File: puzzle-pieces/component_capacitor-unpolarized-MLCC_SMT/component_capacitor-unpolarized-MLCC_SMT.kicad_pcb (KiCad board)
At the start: 2 copper layers, 40 x 40 mm, 34 parts, among them J1 Conn_01x02_Pin, J2 Conn_01x02_Pin

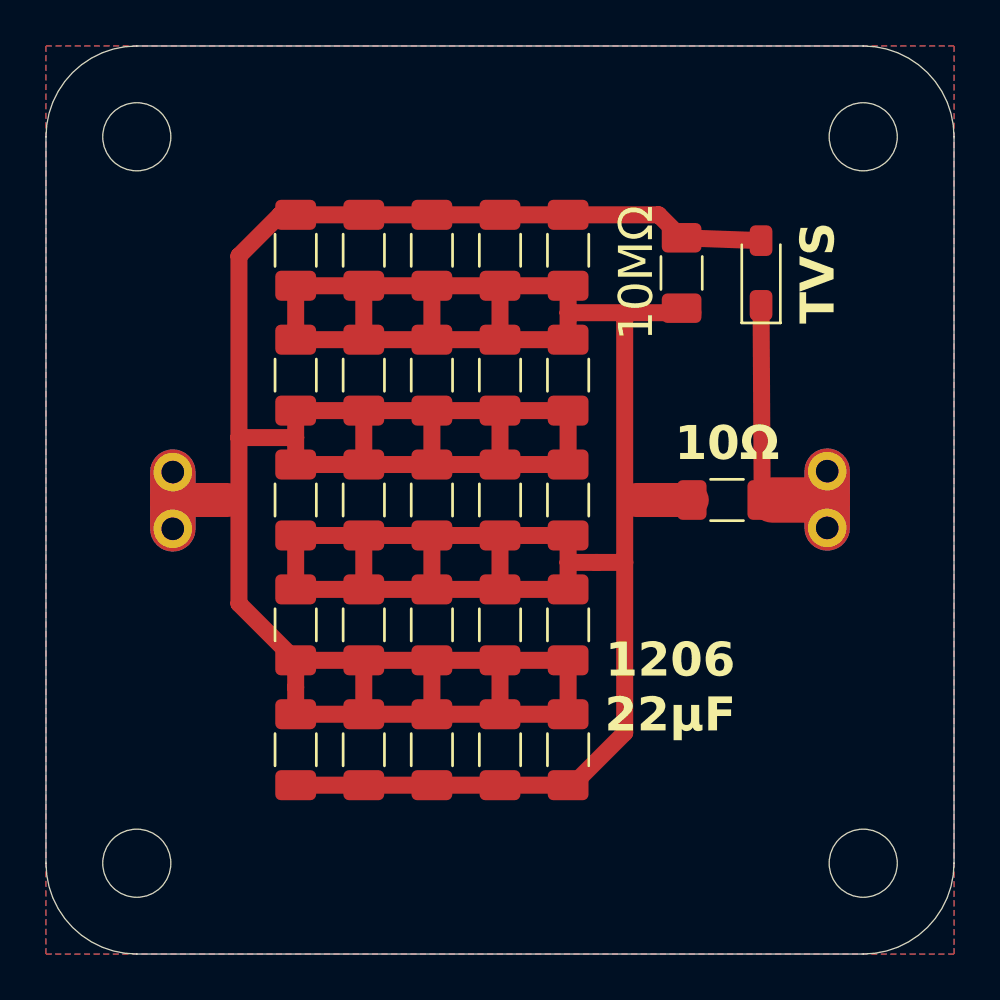
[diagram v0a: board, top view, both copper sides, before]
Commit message: Update unpolarized MLCC SMT components and kicad-viewer configuration
- Updated bottom and top PNG images for the unpolarized MLCC SMT component.
- Updated the ZIP file for the unpolarized MLCC SMT production assets.
- Modified kicad-viewer.json to include "fp_text" and "fp_values" layers in the rendering configuration.
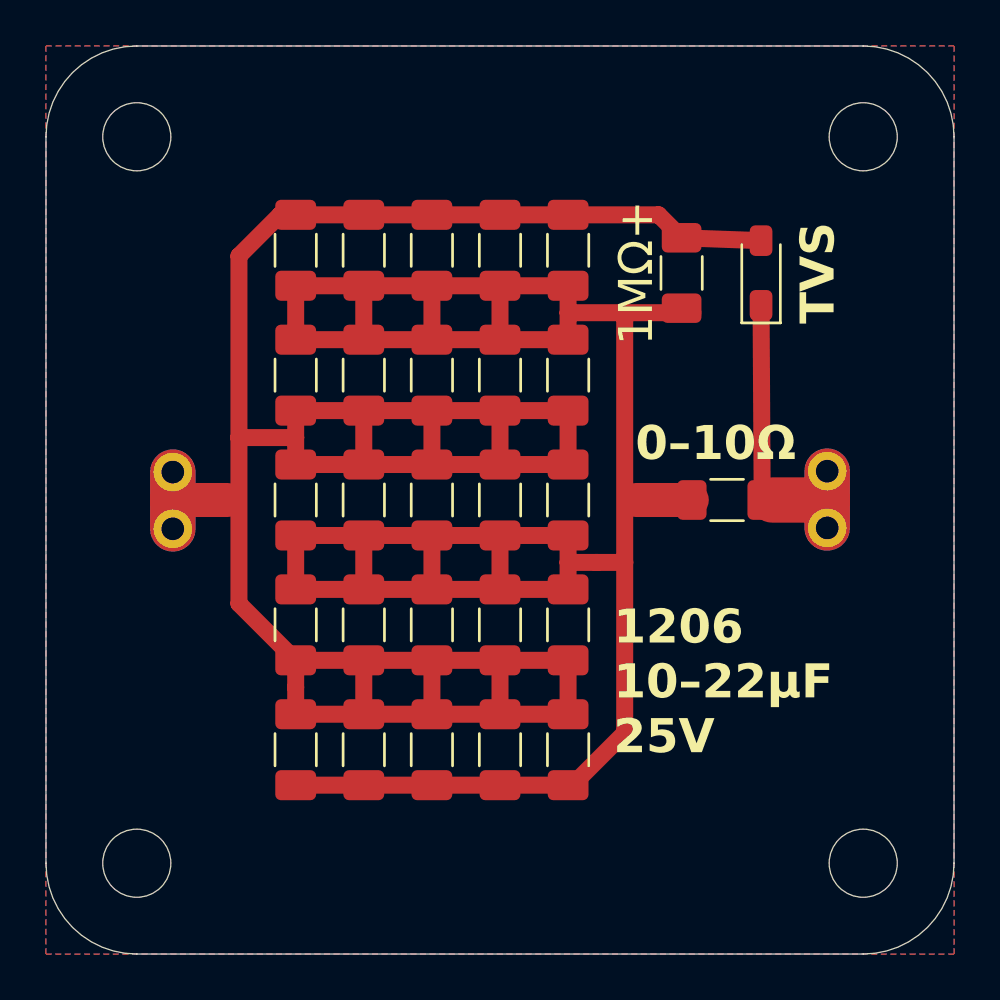
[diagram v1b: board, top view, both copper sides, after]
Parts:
- R1: value 10Ω -> 0–10Ω
- R2: value 10MΩ -> 1MΩ+
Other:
- board text added: "1206 10–22µF 25V"
- board text removed: "1206 22µF"
